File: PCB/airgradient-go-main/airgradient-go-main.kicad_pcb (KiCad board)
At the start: 4 copper layers, 62.9 x 87 mm, 165 parts, among them CN1 SM02B-SRSS-TB (LF)(SN), CN2 BM05B-SRSS-TB(LF)(SN), CN3 BM05B-SRSS-TB(LF)(SN), CN4 HCZZ0039-4, Q1 SIA445EDJ-T1-GE3, Q2 ZVN4106FTA_C508255, Q3 SS8050-G, Q4 SI1308EDL, SW1 TS-1091C-A1B3-D2, SW2 TS-1091C-A1B3-D2, U1 W25N512GVEIG, U10 TMUX121NKGR_C22428404, U11 LIS2DH12TR, U12 HYG-8503A, U13 SHT4x, U14 ZDSD512MLGEAG, U15 DPS368XTSA1, U16 TAU1113, U17 S12, U18 TCA9536DTMR, U2 TPS63802DLAR, U3 BQ25628RYKR, U4 ESP32-C5-MINI-1, U5 TPL5010DDCR, U7 TPS7A0228DQNR, U8 BQ27427YZFR, U9 SGP41-D-R4

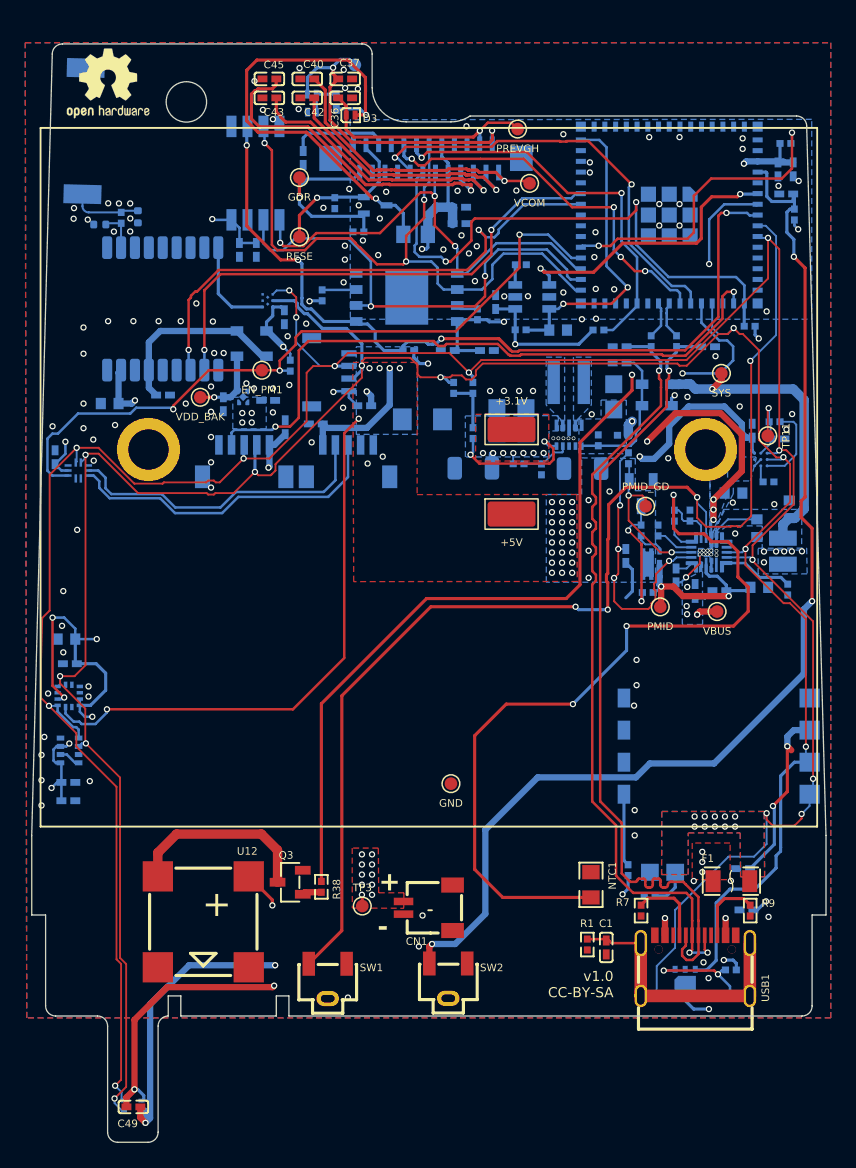
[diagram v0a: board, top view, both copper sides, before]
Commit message: Import v2.0 development state from Bitbucket branch v2.0
Overlay of the v2.0 design work onto the restructured PCB/ layout:
- airgradient-go-main v2.0 WIP: 186 footprints, microSD, PS1-CO,
  Birdy schematic review fixes; adds v2.0 BOM CSVs
- touch-pad v2.0: T1-T3 pads wired to touch controller CS channels,
  +3.1V rail renamed to VCC
- scd4x-module: minor updates
- libraries: new parts (SPL07-003, BM05B-SRSS-TB, PS1-CO, battery
  holder, ESP32-C5 models) and updated footprints; all library and
  3D model references normalized to ${KIPRJMOD}-relative paths
- led_pcb board was dropped in v2.0 (never migrated)

Known open items carried over from review: U14 VDD_IO not yet
connected to the 3.1V rail; U19 (LM66200) still fitted.
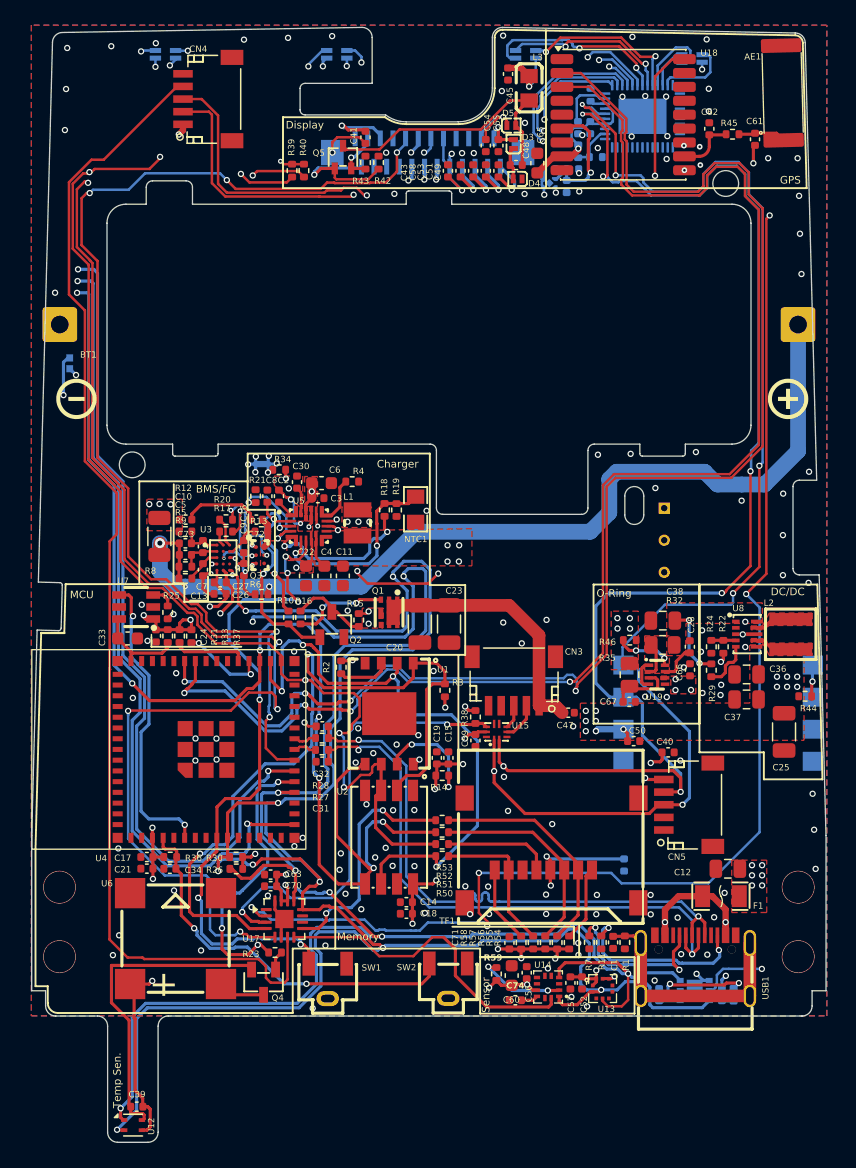
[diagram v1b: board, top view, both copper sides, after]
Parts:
- removed ANT1: GPS1003, easyeda2kicad:ANT-SMD_L10.0-W3.0
- removed CN1: SM02B-SRSS-TB (LF)(SN), easyeda2kicad:CONN-SMD_2P-P1.00_SM02B-SRSS-TB-LF-SN
- removed CN2: BM05B-SRSS-TB(LF)(SN), easyeda2kicad:CONN-SMD-5P-P1.00_BM05B-SRSS-TB-LF-SN
- removed D1, D2: PMEG3005EL,315, easyeda2kicad:SOD-882_L1.0-W0.6-RD
- removed D6, D7: CUS10S30,H3F, easyeda2kicad:SOD-323_L1.8-W1.3-LS2.5-RD
- removed the REF** at (106.6, 63.2)
- removed the REF** at (102.7, 126.9)
- removed the REF** at (134.0, 88.4)
- removed the REF** at (161.2, 126.9)
- removed TAB_BOTTOM, TAB_LEFT, TAB_RIGHT, TAB_TOP: Tab, Tab
- removed TP1: SYS, TestPoint:TestPoint_Pad_D1.0mm
- removed TP10: VDD_BAK, TestPoint:TestPoint_Pad_D1.0mm
- removed TP11: V1.8, TestPoint:TestPoint_Pad_D1.0mm
- removed TP13: GDR, TestPoint:TestPoint_Pad_D1.0mm
- removed TP14: RESE, TestPoint:TestPoint_Pad_D1.0mm
- removed TP15: PREVGH, TestPoint:TestPoint_Pad_D1.0mm
- removed TP16: PREVGL, TestPoint:TestPoint_Pad_D1.0mm
- removed TP17: VCOM, TestPoint:TestPoint_Pad_D1.0mm
- removed TP18: GND, TestPoint:TestPoint_Pad_D1.0mm
- removed TP3: PACK+, TestPoint:TestPoint_Pad_D1.0mm
- removed TP4: PMID_GD, TestPoint:TestPoint_Pad_D1.0mm
- removed TP5: +3.1V, TestPoint:TestPoint_Keystone_5019_Miniature
- removed TP6: PMID, TestPoint:TestPoint_Pad_D1.0mm
- removed TP7: VBUS, TestPoint:TestPoint_Pad_D1.0mm
- removed TP8: +5V, TestPoint:TestPoint_Keystone_5019_Miniature
- removed TP9: EN_PM1, TestPoint:TestPoint_Pad_D1.0mm
- added ?: , , F.Cu at (161.2, 132.4)
- added ?: , , F.Cu at (102.7, 132.4)
- added AE1: Antenna, AG-lib-oaf:CA-G01, F.Cu at (162.9, 63.9)
- added BT1: Battery_Cell, AG-lib-oaf:AGGO-battery, F.Cu at (131.0, 89.7)
- added C44: 1uF/50V, Capacitor_SMD:C_0402_1005Metric, B.Cu at (150.2, 135.4)
- added C61: DNP, Capacitor_SMD:C_0402_1005Metric, F.Cu at (157.8, 67.7)
- added C62: DNP, Capacitor_SMD:C_0402_1005Metric, F.Cu at (154.2, 66.8)
- added C63: 0.1uF/25V, Capacitor_SMD:C_0402_1005Metric, F.Cu at (119.4, 125.9)
- added C64: 1uF/50V, Capacitor_SMD:C_0402_1005Metric, B.Cu at (142.9, 71.4)
- added C65: 10uF/25V, Capacitor_SMD:C_0603_1608Metric, F.Cu at (140.6, 69.5)
- added C66: 1uF/50V, Capacitor_SMD:C_0402_1005Metric, F.Cu at (152.6, 109.7)
- added C67: 1uF/50V, Capacitor_SMD:C_0402_1005Metric, F.Cu at (147.8, 112.2)
- added C68: 1uF/50V, Capacitor_SMD:C_0402_1005Metric, B.Cu at (143.8, 66.7)
- added C69: 0.1uF/16V, Capacitor_SMD:C_0402_1005Metric, B.Cu at (144.7, 66.7)
- added C70: 0.1uF/25V, Capacitor_SMD:C_0402_1005Metric, F.Cu at (119.4, 126.8)
- added C71: 0.1uF/25V, Capacitor_SMD:C_0402_1005Metric, F.Cu at (138.3, 131.3)
- added C72: 0.1uF/25V, Capacitor_SMD:C_0402_1005Metric, F.Cu at (118.3, 97.8)
- added C73: 0.1uF/25V, Capacitor_SMD:C_0402_1005Metric, F.Cu at (112.7, 97.8)
- added C74: 0.1uF/25V, Capacitor_SMD:C_0402_1005Metric, F.Cu at (138.8, 135.8)
- added CN5: SM05B-SRSS-TB (LF)(SN), easyeda2kicad-oaf:CONN-SMD_SM05B-SRSS-TB-LF-SN, F.Cu at (152.5, 120.3)
- added G***: LOGO, LOGO, F.Cu at (160.4, 88.2)
- added G***: LOGO, LOGO, F.Cu at (104.1, 88.2)
- added G***: LOGO, LOGO, B.Cu at (160.4, 88.2)
- added G***: LOGO, LOGO, B.Cu at (104.1, 88.2)
- added LED1: TJ-S1608SW6TDSLCCYRGB-A5, easyeda2kicad-oaf:LED-ARRAY-SMD_4P-L1.6-W0.8-BL-FD, B.Cu at (111.1, 60.9)
- added LED2: TJ-S1608SW6TDSLCCYRGB-A5, easyeda2kicad-oaf:LED-ARRAY-SMD_4P-L1.6-W0.8-BL-FD, B.Cu at (124.7, 60.9)
- added LED3: TJ-S1608SW6TDSLCCYRGB-A5, easyeda2kicad-oaf:LED-ARRAY-SMD_4P-L1.6-W0.8-BL-FD, B.Cu at (139.6, 60.9)
- added LED4: TJ-S1608SW6TDSLCCYRGB-A5, easyeda2kicad-oaf:LED-ARRAY-SMD_4P-L1.6-W0.8-BL-FD, B.Cu at (152.8, 61.2)
- added NT1: NetTie_2, NetTie:NetTie-2_SMD_Pad0.5mm, B.Cu at (118.7, 93.4)
- added NTC2: NCP15XH103F03RC, easyeda2kicad-oaf:R0402, B.Cu at (103.5, 85.4)
- added Q5: SI1308EDL, easyeda2kicad-oaf:SOT-323-3_L2.0-W1.3-P1.30-LS2.1-BR, F.Cu at (125.2, 69.1)
- added R15: 15K, Resistor_SMD:R_0402_1005Metric, F.Cu at (126.4, 105.7)
- added R40: 100K, Resistor_SMD:R_0402_1005Metric, F.Cu at (122.1, 70.1)
- added R41: 4.7R, Resistor_SMD:R_0402_1005Metric, B.Cu at (156.1, 135.4)
- added R42: 1M, Resistor_SMD:R_0402_1005Metric, F.Cu at (128.0, 69.5)
- added R43: 2.2R, Resistor_SMD:R_0402_1005Metric, F.Cu at (126.9, 69.5)
- added R44: 100K, Resistor_SMD:R_0402_1005Metric, F.Cu at (161.8, 111.8)
- added R45: 0R, Resistor_SMD:R_0402_1005Metric, F.Cu at (156.0, 67.2)
- added R46: 100K, Resistor_SMD:R_0402_1005Metric, F.Cu at (147.9, 107.3)
- added R47: 0R, Resistor_SMD:R_0402_1005Metric, B.Cu at (143.8, 68.6)
- added R48: 0R, Resistor_SMD:R_0402_1005Metric, B.Cu at (145.2, 69.1)
- added R49: 5.1K, Resistor_SMD:R_0402_1005Metric, B.Cu at (144.8, 64.1)
- added R50: 22R, Resistor_SMD:R_0402_1005Metric, F.Cu at (133.0, 124.4)
- added R51: 22R, Resistor_SMD:R_0402_1005Metric, F.Cu at (133.0, 123.5)
- added R52: 22R, Resistor_SMD:R_0402_1005Metric, F.Cu at (133.0, 122.5)
- added R53: 22R, Resistor_SMD:R_0402_1005Metric, F.Cu at (133.0, 121.6)
- added R54: 10K, Resistor_SMD:R_0402_1005Metric, F.Cu at (143.1, 131.3)
- added R55: 10K, Resistor_SMD:R_0402_1005Metric, F.Cu at (142.1, 131.3)
- added R56: 10K, Resistor_SMD:R_0402_1005Metric, F.Cu at (141.2, 131.3)
- added R57: 10K, Resistor_SMD:R_0402_1005Metric, F.Cu at (140.2, 131.3)
- added R58: 10K, Resistor_SMD:R_0402_1005Metric, F.Cu at (139.3, 131.3)
- added R59: 100K, Resistor_SMD:R_0402_1005Metric, F.Cu at (137.3, 133.8)
- added TF1: TF-CARD XG8P H1.5, easyeda2kicad-oaf:TF-SMD_TF-CARD-XG8P-H1.5, F.Cu at (141.7, 124.0)
- added U19: LM66200DRLR, easyeda2kicad-oaf:SOT-583-8_L2.1-W1.2-P0.50-LS1.6-BL, F.Cu at (150.0, 110.1)
- added U20: LP5036, Package_DFN_QFN:VQFN-46-1EP_5x6mm_P0.4mm_EP2.8x3.8mm, B.Cu at (148.9, 65.8)
- added U6: HYG-8503A, easyeda2kicad-oaf:BUZ-SMD_4P-L8.5-W8.5-P8.50-BR, F.Cu at (111.9, 130.9)
- C1, C35, C40, C43: footprint easyeda2kicad:C0402 -> Capacitor_SMD:C_0402_1005Metric
- C10, C7: value 10uF/10V -> 0.1uF/25V; footprint easyeda2kicad:C0402 -> Capacitor_SMD:C_0402_1005Metric; moved to F.Cu
- C11, C4: footprint easyeda2kicad:C0603 -> Capacitor_SMD:C_0603_1608Metric; moved to F.Cu
- C12: value 0.1uF/25V -> 22uF/25V; footprint easyeda2kicad:C0402 -> Capacitor_SMD:C_0805_2012Metric; moved to F.Cu
- C13, C5: value 22uF/25V -> 0.1uF/25V; footprint easyeda2kicad:C0805 -> Capacitor_SMD:C_0402_1005Metric; moved to F.Cu
- C14, C19, C2, C26, C41, C55: footprint easyeda2kicad:C0402 -> Capacitor_SMD:C_0402_1005Metric; moved to F.Cu
- C15, C3, C59: value 10uF/25V -> 0.1uF/25V; footprint easyeda2kicad:C0603 -> Capacitor_SMD:C_0402_1005Metric; moved to F.Cu
- C16: value 4.7uF/25V -> 0.1uF/25V; footprint easyeda2kicad:C0402 -> Capacitor_SMD:C_0402_1005Metric; moved to F.Cu
- C17: value 22uF/25V -> 0.1uF/10V; footprint easyeda2kicad:C0805 -> Capacitor_SMD:C_0402_1005Metric; moved to F.Cu
- C18: value DNP -> 1uF/50V; footprint Capacitor_SMD:C_1206_3216Metric -> Capacitor_SMD:C_0402_1005Metric; moved to F.Cu
- C20: footprint easyeda2kicad:C1206 -> Capacitor_SMD:C_1206_3216Metric; moved to F.Cu
- C21: value 1nF/50V -> 22uF/10V; footprint easyeda2kicad:C0402 -> Capacitor_SMD:C_0402_1005Metric; moved to F.Cu
- C22: value 1nF/50V -> 10uF/25V; footprint easyeda2kicad:C0402 -> Capacitor_SMD:C_0603_1608Metric; moved to F.Cu
- C23: value 500pF/50V -> DNP; footprint easyeda2kicad:C0603 -> Capacitor_SMD:C_1206_3216Metric; moved to F.Cu
- C24: value DNP -> 0.1uF/25V; footprint Capacitor_SMD:C_1206_3216Metric -> Capacitor_SMD:C_0402_1005Metric; moved to F.Cu
- C25: value 10nF/10V -> DNP; footprint easyeda2kicad:C0402 -> Capacitor_SMD:C_1206_3216Metric; moved to F.Cu
- C27: value 1uF/50V -> 0.47uF/25V; footprint easyeda2kicad:C0402 -> Capacitor_SMD:C_0402_1005Metric; moved to F.Cu
- C28: value 2.2uF/16V -> 0.1uF/25V; footprint easyeda2kicad:C0402 -> Capacitor_SMD:C_0402_1005Metric; moved to F.Cu
- C29, C46, C49: value 0.1uF/25V -> 1uF/50V; footprint easyeda2kicad:C0402 -> Capacitor_SMD:C_0402_1005Metric
- C30: value 4.7uF/25V -> 1uF/50V; footprint easyeda2kicad:C0402 -> Capacitor_SMD:C_0402_1005Metric; moved to F.Cu
- C31: value 1uF/50V -> 1nF/50V; footprint easyeda2kicad:C0402 -> Capacitor_SMD:C_0402_1005Metric; moved to F.Cu
- C32: value 4.7uF/25V -> 1nF/50V; footprint easyeda2kicad:C0402 -> Capacitor_SMD:C_0402_1005Metric; moved to F.Cu
- C33: value 0.1uF/25V -> 500pF/50V; footprint easyeda2kicad:C0402 -> Capacitor_SMD:C_0603_1608Metric; moved to F.Cu
- C34: value 1uF/50V -> 10nF/10V; footprint easyeda2kicad:C0402 -> Capacitor_SMD:C_0402_1005Metric; moved to F.Cu
- C36, C37: value 1uF/50V -> 22uF/25V; footprint easyeda2kicad:C0402 -> Capacitor_SMD:C_0805_2012Metric
- C38: value 1uF/50V -> 22uF/25V; footprint easyeda2kicad:C0402 -> Capacitor_SMD:C_0805_2012Metric; moved to F.Cu
- C39, C52, C56, C57, C9: value 1uF/50V -> 0.1uF/25V; footprint easyeda2kicad:C0402 -> Capacitor_SMD:C_0402_1005Metric; moved to F.Cu
- C42: footprint easyeda2kicad:C0402 -> Capacitor_SMD:C_0402_1005Metric; moved to B.Cu
- C45: value 1uF/50V -> 4.7uF/25V; footprint easyeda2kicad:C0402 -> Capacitor_SMD:C_0402_1005Metric
- C47, C51: value DNP -> 1uF/50V; moved to F.Cu
- C48: value 1uF/50V -> 4.7uF/25V; footprint easyeda2kicad:C0402 -> Capacitor_SMD:C_0402_1005Metric; moved to F.Cu
- C50, C54, C58: value 0.1uF/25V -> 1uF/50V; footprint easyeda2kicad:C0402 -> Capacitor_SMD:C_0402_1005Metric; moved to F.Cu
- C53: value 10uF/25V -> 1uF/50V; footprint easyeda2kicad:C0603 -> Capacitor_SMD:C_0402_1005Metric; moved to F.Cu
- C6, C60: value 0.1uF/25V -> 10uF/25V; footprint easyeda2kicad:C0402 -> Capacitor_SMD:C_0603_1608Metric; moved to F.Cu
- C8: value 22uF/25V -> 4.7uF/25V; footprint easyeda2kicad:C0805 -> Capacitor_SMD:C_0402_1005Metric; moved to F.Cu
- CN3: value BM05B-SRSS-TB(LF)(SN) -> SM05B-SRSS-TB (LF)(SN); footprint easyeda2kicad:CONN-SMD-5P-P1.00_BM05B-SRSS-TB-LF-SN -> easyeda2kicad-oaf:CONN-SMD_SM05B-SRSS-TB-LF-SN; moved to F.Cu
- CN4: value HCZZ0039-4 -> SM05B-SRSS-TB (LF)(SN); footprint easyeda2kicad:CONN-SMD_HCZZ0039-4 -> easyeda2kicad-oaf:CONN-SMD_SM05B-SRSS-TB-LF-SN; moved to F.Cu
- D3: footprint easyeda2kicad:SOD-882_L1.0-W0.6-RD -> easyeda2kicad-oaf:SOD-882_L1.0-W0.6-RD
- D4, D5: value CUS10S30,H3F -> PMEG3005EL,315; footprint easyeda2kicad:SOD-323_L1.8-W1.3-LS2.5-RD -> easyeda2kicad-oaf:SOD-882_L1.0-W0.6-RD; moved to F.Cu
- F1: footprint easyeda2kicad:F1206 -> easyeda2kicad-oaf:F1206
- FPC1: footprint easyeda2kicad:FPC-SMD_FPC-0.5-24P-LTH2.0 -> easyeda2kicad-oaf:FPC-SMD_FPC-0.5-24P-LTH2.0
- L1: footprint easyeda2kicad:IND-SMD_L2.5-W2.0 -> easyeda2kicad-oaf:IND-SMD_L2.5-W2.0; moved to F.Cu
- L2: footprint easyeda2kicad:IND-SMD_L4.0-W4.0_XGL4020 -> easyeda2kicad-oaf:IND-SMD_L4.0-W4.0_XGL4020; moved to F.Cu
- L3: footprint easyeda2kicad:L0805 -> easyeda2kicad-oaf:L0805; moved to F.Cu
- NTC1: footprint easyeda2kicad:R0805 -> easyeda2kicad-oaf:R0805
- Q1: footprint easyeda2kicad:SC-70-6L_L2.0-W2.0-P0.65-BL -> easyeda2kicad-oaf:SC-70-6L_L2.0-W2.0-P0.65-BL; moved to F.Cu
- Q2: footprint easyeda2kicad:SOT-23-3_L2.9-W1.3-P1.90-LS2.4-BR -> easyeda2kicad-oaf:SOT-23-3_L2.9-W1.3-P1.90-LS2.4-BR; moved to F.Cu
- Q3: value SS8050-G -> CSD83325L; footprint easyeda2kicad:SOT-23-3_L2.9-W1.3-P1.90-LS2.4-BR -> easyeda2kicad-oaf:PICOSTAR-6_L2.2-W1.1-R2-C3-P0.65-BL
- Q4: value SI1308EDL -> SS8050-G; footprint easyeda2kicad:SOT-323-3_L2.0-W1.3-P1.30-LS2.1-BR -> easyeda2kicad-oaf:SOT-23-3_L2.9-W1.3-P1.90-LS2.4-BR; moved to F.Cu
- R1, R7: footprint easyeda2kicad:R0402 -> Resistor_SMD:R_0402_1005Metric
- R10, R14, R2, R26, R3, R30, R31, R33, R36, R37: footprint easyeda2kicad:R0402 -> Resistor_SMD:R_0402_1005Metric; moved to F.Cu
- R11: value 4.12K -> 5.1K; footprint easyeda2kicad:R0402 -> Resistor_SMD:R_0402_1005Metric; moved to F.Cu
- R12: value 17.33K -> 200R; footprint easyeda2kicad:R0402 -> Resistor_SMD:R_0402_1005Metric; moved to F.Cu
- R13: value 2.49K -> 2K; footprint easyeda2kicad:R0402 -> Resistor_SMD:R_0402_1005Metric; moved to F.Cu
- R16: value 51K -> 20K; footprint easyeda2kicad:R0402 -> Resistor_SMD:R_0402_1005Metric; moved to F.Cu
- R17: value 15K -> 1K; footprint easyeda2kicad:R0402 -> Resistor_SMD:R_0402_1005Metric; moved to F.Cu
- R18: value 20K -> 4.12K; footprint easyeda2kicad:R0402 -> Resistor_SMD:R_0402_1005Metric; moved to F.Cu
- R19: value 10K -> 17.33K; footprint easyeda2kicad:R0402 -> Resistor_SMD:R_0402_1005Metric; moved to F.Cu
- R20: value 22R -> 1K; footprint easyeda2kicad:R0402 -> Resistor_SMD:R_0402_1005Metric; moved to F.Cu
- R21: value 22R -> 2.49K; footprint easyeda2kicad:R0402 -> Resistor_SMD:R_0402_1005Metric; moved to F.Cu
- R22: value 10K -> 475K; footprint easyeda2kicad:R0402 -> Resistor_SMD:R_0402_1005Metric; moved to F.Cu
- R23: value 100K -> 1K; footprint easyeda2kicad:R0402 -> Resistor_SMD:R_0402_1005Metric; moved to F.Cu
- R24: value 10K -> 91K; footprint easyeda2kicad:R0402 -> Resistor_SMD:R_0402_1005Metric; moved to F.Cu
- R25: value 0R -> 51K; footprint easyeda2kicad:R0402 -> Resistor_SMD:R_0402_1005Metric; moved to F.Cu
- R27, R28: value 10K -> 22R; footprint easyeda2kicad:R0402 -> Resistor_SMD:R_0402_1005Metric; moved to F.Cu
- R29, R39: value 0R -> 100K; footprint easyeda2kicad:R0402 -> Resistor_SMD:R_0402_1005Metric; moved to F.Cu
- R32: value 1M -> 50mR; footprint easyeda2kicad:R0402 -> Resistor_SMD:R_0805_2012Metric; moved to F.Cu
- R34: value 2.2R -> 10K; footprint easyeda2kicad:R0402 -> Resistor_SMD:R_0402_1005Metric; moved to F.Cu
- R35: value 4.7R -> 470mR; footprint easyeda2kicad:R0402 -> Resistor_SMD:R_0805_2012Metric; moved to F.Cu
- R38: value 1K -> 100K; footprint easyeda2kicad:R0402 -> Resistor_SMD:R_0402_1005Metric
- R4: value 475K -> 100K; footprint easyeda2kicad:R0402 -> Resistor_SMD:R_0402_1005Metric; moved to F.Cu
- R5: value 100K -> 200R; footprint easyeda2kicad:R0402 -> Resistor_SMD:R_0402_1005Metric; moved to F.Cu
- R6: value 91K -> 10R; footprint easyeda2kicad:R0402 -> Resistor_SMD:R_0402_1005Metric; moved to F.Cu
- R8: value 100K -> 5mR 1%/1W; footprint easyeda2kicad:R0402 -> Resistor_SMD:R_1206_3216Metric; moved to F.Cu
- R9: value 5.1K -> 10R; footprint easyeda2kicad:R0402 -> Resistor_SMD:R_0402_1005Metric
- REF**: footprint AG-lib:GO-enclosure -> AG-lib-oaf:GO-enclosure
- REF**: footprint SPS30:SPS30 -> SPS30-oaf:SPS30
- SW1, SW2: footprint easyeda2kicad:KEY-SMD_3P-L5.5-W3.8-P3.00 -> easyeda2kicad-oaf:KEY-SMD_3P-L5.5-W3.8-P3.00
- U1: footprint easyeda2kicad:WSON-8_L8.0-W6.0-P1.27-TL-1 -> easyeda2kicad-oaf:WSON-8_L8.0-W6.0-P1.27-TL-1; moved to F.Cu
- U10: value TMUX121NKGR_C22428404 -> SGP41-D-R4; footprint easyeda2kicad:UQFN-10_L1.8-W1.4-P0.40-BL -> Senserion-oaf:XDCR_SGP41-D-R4
- U11: value LIS2DH12TR -> PS1-CO-SMOKE-10k; footprint easyeda2kicad:LGA-12_L2.0-W2.0-P0.50-BL -> AG-lib-oaf:PS1-CO-SMOKE-10k
- U12: value HYG-8503A -> SHT4x; footprint easyeda2kicad:BUZ-SMD_4P-L8.5-W8.5-P8.50-BR -> Sensor_Humidity:Sensirion_DFN-4_1.5x1.5mm_P0.8mm_SHT4x_NoCentralPad
- U13: value SHT4x -> SPL07-003; footprint Sensor_Humidity:Sensirion_DFN-4_1.5x1.5mm_P0.8mm_SHT4x_NoCentralPad -> easyeda2kicad-oaf:LGA-10_L2.0-W2.0-P0.50-BL; moved to F.Cu
- U14: value ZDSD512MLGEAG -> LIS2DH12TR; footprint easyeda2kicad:LGA-8_L8.0-W6.0-P1.27-TL -> easyeda2kicad-oaf:LGA-12_L2.0-W2.0-P0.50-BL; moved to F.Cu
- U15: value DPS368XTSA1 -> TMUX121NKGR_C22428404; footprint easyeda2kicad:LGA-8_L2.5-W2.0-P0.65-TR_DPS368 -> easyeda2kicad-oaf:UQFN-10_L1.8-W1.4-P0.40-BL; moved to F.Cu
- U16: value TAU1113 -> S12; footprint RF_GPS:TAU1113 -> S12-oaf:S12
- U17: value S12 -> TCA6408ARGT; footprint S12:S12 -> Package_DFN_QFN:VQFN-16-1EP_3x3mm_P0.5mm_EP1.45x1.45mm; moved to F.Cu
- U18: value TCA9536DTMR -> TAU1113; footprint easyeda2kicad:X2SON-8_L1.4-W0.8-P0.50-BL -> RF_GPS-oaf:TAU1113; moved to F.Cu
- U2: value TPS63802DLAR -> ZDSD512MLGEAG; footprint easyeda2kicad:VSON-10_L3.0-W2.0-P0.50-TL -> easyeda2kicad-oaf:LGA-8_L8.0-W6.0-P1.27-TL; moved to F.Cu
- U3: value BQ25628RYKR -> BQ27742YZFR-G1; footprint easyeda2kicad:WQFN-18_L3.0-W2.5-P0.40-TL -> easyeda2kicad-oaf:DSBGA-15_L2.6-W2.0-R5-C3-P0.50-BL; moved to F.Cu
- U4: footprint Esparessif:ESP32-C5-MINI-1 -> Esparessif-oaf:ESP32-C5-MINI-1; moved to F.Cu
- U5: value TPL5010DDCR -> BQ25628RYKR; footprint easyeda2kicad:SOT-23-6_L2.9-W1.6-P0.95-LS2.8-BR -> easyeda2kicad-oaf:WQFN-18_L3.0-W2.5-P0.40-TL; moved to F.Cu
- U7: value TPS7A0228DQNR -> TPL5010DDCR; footprint easyeda2kicad:X2SON-4_L1.0-W1.0-P0.65-TL-EP -> easyeda2kicad-oaf:SOT-23-6_L2.9-W1.6-P0.95-LS2.8-BR; moved to F.Cu
- U8: value BQ27427YZFR -> TPS63802DLAR; footprint easyeda2kicad:DSBGA-9_L1.6-W1.6-R3-C3-P0.50-TL -> easyeda2kicad-oaf:VSON-10_L3.0-W2.0-P0.50-TL; moved to F.Cu
- U9: value SGP41-D-R4 -> TPS7A0228DQNR; footprint Senserion:XDCR_SGP41-D-R4 -> easyeda2kicad-oaf:X2SON-4_L1.0-W1.0-P0.65-TL-EP
- USB1: footprint easyeda2kicad:USB-C-SMD_G-SWITCH_GT-USB-7010ASV -> easyeda2kicad-oaf:USB-C-SMD_G-SWITCH_GT-USB-7010ASV
- moved C49 79.6 mm to (137.5, 70.2), turned to -90 degrees
- moved U14 68.5 mm to (141.4, 134.8), turned to 90 degrees
- moved C41 68.2 mm to (126.9, 67.5), turned to 90 degrees
- moved R26 68.1 mm to (116.7, 125.4), turned to 0 degrees
- moved C46 67.8 mm to (155.2, 135.4)
- moved U4 66.7 mm to (106.6, 115.8), turned to 90 degrees
- moved C42 65.7 mm to (147.4, 125.1), turned to 90 degrees
- moved U9 64.3 mm to (141.5, 71.1), turned to 180 degrees
- moved U10 63.9 mm to (153.0, 135.1)
- moved Q4 62.2 mm to (118.9, 134.4), turned to 90 degrees
- moved U11 60.9 mm to (163.1, 99.4), turned to -90 degrees
- moved C21 60.7 mm to (109.6, 125.4), turned to 0 degrees
- moved C40 60.5 mm to (150.9, 116.2), turned to 180 degrees
- moved C58 58.8 mm to (134.5, 70.2), turned to -90 degrees
- moved C37 58.5 mm to (157.1, 112.0), turned to 0 degrees
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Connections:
- C10 pad 1: GND -> Net-(U3-SRP)
- C10 pad 2: +3.1V -> /BAT+
- C11 pad 2: Load+ -> SYS
- C12 pad 2: PMID -> VBUS
- C13 pad 1: GND -> Net-(U3-VPWR)
- C13 pad 2: +3.1V -> /BAT-
- C15 pad 2: PMID -> +3.1V
- C16 pad 1: GND -> Net-(U3-PACKP)
- C16 pad 2: /REGN -> /BAT-
- C17 pad 2: Net-(U2-VIN) -> +3.1V
- C18 pad 1: +3.1V -> GND
- C18 pad 2: GND -> +3.1V
- C19 pad 2: VBUS -> +3.1V
- C21 pad 2: /USB_D- -> +3.1V
- C22 pad 2: /USB_D+ -> Pack+
- C23 pad 1: GND -> +5V
- C23 pad 2: /EN -> GND
- C24 pad 1: +5V -> GND
- C24 pad 2: GND -> +3.1V
- C25 pad 1: GND -> +3.1V
- C25 pad 2: /IO28 -> GND
- C26 pad 1: GND -> /BAT-
- C26 pad 2: PACK+ -> Net-(U3-REG25)
- C27 pad 1: GND -> Net-(U3-REG25)
- C27 pad 2: VDD_BAK -> Net-(U3-TS)
- C28 pad 1: V1.8 -> GND
- C28 pad 2: GND -> Net-(C28-Pad2)
- C29 pad 2: Net-(D6-K) -> VDD_BAK
- C3 pad 2: SYS -> PMID
- C30 pad 2: +3.1V -> VBUS
- C31 pad 2: Load+ -> /USB_D-
- C32 pad 1: Net-(Q4-D) -> GND
- C32 pad 2: Net-(C32-Pad2) -> /USB_D+
- C33 pad 2: +3.1V -> /EN
- C34 pad 2: Net-(C34-Pad2) -> /IO28
- C35 pad 2: +3.1V -> Pack+
- C36 pad 2: /PREVGH -> +3.1V
- C37 pad 2: /PREVGL -> +3.1V
- C38 pad 2: +3.1V -> Net-(U8-EN)
- C39 pad 2: Net-(U9-VDD) -> +3.1V
- C40 pad 2: /VCOM -> +3.1V
- C41 pad 2: +3.1V -> Net-(C41-Pad2)
- C42 pad 2: Net-(C42-Pad2) -> +3.1V
- C43 pad 2: Net-(C43-Pad2) -> +3.1V
- C45 pad 2: Net-(C45-Pad2) -> +3.1V
- C47 pad 1: Net-(ANT1-Pad1) -> GND
- C47 pad 2: GND -> +5V
- C48 pad 1: GND -> Net-(Q5-D)
- C48 pad 2: +3.1V -> Net-(C48-Pad2)
- C49 pad 2: +3.1V -> /VCOM
- C5 pad 1: GND -> /BAT+
- C5 pad 2: VBUS -> Net-(U3-SRN)
- C51 pad 1: /GNSS_RF -> GND
- C51 pad 2: GND -> Net-(C51-Pad2)
- C53 pad 2: +3.1V -> Net-(C53-Pad2)
- C54 pad 2: +3.1V -> /PREVGH
- C55 pad 2: Net-(D4-K) -> /PREVGL
- C56 pad 2: +5V -> +3.1V
- C58 pad 2: +3.1V -> Net-(C58-Pad2)
- C6 pad 2: +3.1V -> PMID
- C7 pad 1: GND -> Net-(U3-SRP)
- C7 pad 2: +3.1V -> Net-(U3-SRN)
- C8 pad 2: +3.1V -> /REGN
- C9 pad 1: GND -> Net-(U3-BAT)
- C9 pad 2: +3.1V -> /BAT-
- CN3 pad 1: GND -> +5V
- CN3 pad 2: GND -> /PM_SDA
- CN3 pad 4: /PM_SDA -> GND
- CN3 pad 5: +5V -> GND
- CN4 pad 4: GND -> /INT
- D3 pad 1: /PREVGH -> Net-(C48-Pad2)
- D3 pad 2: Net-(Q4-D) -> /PREVGL
- D4 pad 1: Net-(D4-K) -> GND
- D4 pad 2: VDD_BAK -> Net-(C48-Pad2)
- D5 pad 1: Net-(D4-K) -> /PREVGH
- D5 pad 2: +3.1V -> Net-(Q5-D)
- FPC1 pad 18: Net-(C45-Pad2) -> Net-(C58-Pad2)
- FPC1 pad 20: Net-(C43-Pad2) -> Net-(C53-Pad2)
- FPC1 pad 22: Net-(C42-Pad2) -> Net-(C51-Pad2)
- FPC1 pad 5: Net-(C34-Pad2) -> Net-(C41-Pad2)
- L2 pad 1: Net-(U2-L1) -> Net-(U8-L1)
- L2 pad 2: Net-(U2-L2) -> Net-(U8-L2)
- L3 pad 2: Net-(Q4-D) -> Net-(Q5-D)
- NTC1 pad 2: Net-(U3-TS) -> Net-(U5-TS)
- Q4 pad 1: /GDR -> Net-(Q4-B)
- Q4 pad 2: /RESE -> GND
- Q4 pad 3: Net-(Q4-D) -> Net-(Q4-C)
- R10 pad 1: Net-(U1-/HOLD(IO3)) -> /REGN
- R10 pad 2: +3.1V -> /PMID_GD
- R11 pad 1: Net-(U3-TS) -> GND
- R11 pad 2: Net-(U3-TS_BIAS) -> Net-(USB1-CC2)
- R12 pad 1: GND -> Net-(C73-Pad2)
- R12 pad 2: Net-(U3-TS) -> Net-(U3-SRP)
- R13 pad 1: GND -> Pack+
- R13 pad 2: Net-(U3-ILIM) -> Net-(U3-PACKP)
- R14 pad 1: /REGN -> Net-(U1-/HOLD(IO3))
- R14 pad 2: /PMID_GD -> +3.1V
- R16 pad 1: GND -> Net-(Q2-D)
- R16 pad 2: Net-(U5-DELAY/M_RST) -> Net-(Q1-G)
- R17 pad 1: PMID -> Net-(U3-CHG)
- R17 pad 2: Net-(Q2-D) -> Net-(Q3-G-PadB1)
- R18 pad 1: Net-(Q2-D) -> Net-(U5-TS)
- R18 pad 2: Net-(Q1-G) -> Net-(U5-TS_BIAS)
- R19 pad 1: /SDA -> GND
- R19 pad 2: +3.1V -> Net-(U5-TS)
- R20 pad 1: /USB_D- -> Net-(U3-DSG)
- R20 pad 2: /USB- -> Net-(Q3-G-PadB2)
- R21 pad 1: /USB_D+ -> GND
- R21 pad 2: /USB+ -> Net-(U5-ILIM)
- R22 pad 1: /SCL -> Net-(U8-FB)
- R23 pad 1: /EN -> /BUZZ
- R23 pad 2: +3.1V -> Net-(Q4-B)
- R24 pad 1: /IO27 -> Net-(U8-FB)
- R24 pad 2: +3.1V -> GND
- R25 pad 1: Net-(D6-K) -> GND
- R25 pad 2: Net-(U2-VIN) -> Net-(U7-DELAY/M_RST)
- R26 pad 1: /IO28 -> /SDA
- R27 pad 1: /EN_PM1 -> /USB_D-
- R27 pad 2: +3.1V -> /USB-
- R28 pad 1: Net-(U8-BIN) -> /USB+
- R28 pad 2: GND -> /USB_D+
- R29 pad 1: Net-(U2-VIN) -> Net-(U8-EN)
- R29 pad 2: Load+ -> Net-(U8-PG)
- R30 pad 1: V1.8 -> /SCL
- R30 pad 2: Net-(U8-GPOUT) -> +3.1V
- R31 pad 1: +3.1V -> /EN
- R31 pad 2: /ePaper CS -> +3.1V
- R32 pad 1: GND -> Net-(C28-Pad2)
- R32 pad 2: /GDR -> Net-(U8-EN)
- R33 pad 1: +3.1V -> /IO27
- R33 pad 2: /ePaper D/C -> +3.1V
- R34 pad 2: /RESE -> VBUS
- R35 pad 1: Net-(U9-VDD) -> VBUS
- R35 pad 2: +3.1V -> Net-(U19-VIN1)
- R36 pad 1: GND -> /IO28
- R36 pad 2: VBUS -> +3.1V
- R37 pad 1: Net-(U17-EN) -> /IO26
- R38 pad 1: /BUZZ -> /EN_PM1
- R38 pad 2: Net-(Q3-B) -> +3.1V
- R39 pad 1: Net-(ANT1-Pad1) -> +3.1V
- R39 pad 2: /GNSS_RF -> /ePaper CS
- R4 pad 1: Net-(U2-FB) -> GND
- R4 pad 2: +3.1V -> /CE
- R5 pad 1: GND -> /BAT+
- R5 pad 2: /CE -> Net-(U3-SRN)
- R6 pad 1: Net-(U2-FB) -> /BAT+
- R6 pad 2: GND -> Net-(U3-BAT)
- R8 pad 1: +3.1V -> /BAT+
- R8 pad 2: Net-(U2-PG) -> Net-(C73-Pad2)
- R9 pad 1: GND -> /BAT+
- R9 pad 2: Net-(USB1-CC2) -> Net-(U3-VPWR)
- U10 pad 1: /SCL -> Net-(U10-VDD)
- U10 pad 2: /SDA -> GND
- U10 pad 3: GND -> /SDA
- U10 pad 4: /PM_SDA -> GND
- U10 pad 5: /PM_SCL -> +3.1V
- U10 pad 6: unconnected-(U10-S2B-Pad6) -> /SCL
- U10 pad 7: unconnected-(U10-S1B-Pad7) -> GND
- U11 pad 1: /SCL -> unconnected-(U11-R-Pad1)
- U11 pad 2: +3.1V -> unconnected-(U11-S-Pad2)
- U11 pad 3: GND -> unconnected-(U11-C-Pad3)
- U12 pad 1: +3.1V -> /SDA
- U12 pad 2: Net-(Q3-C) -> /SCL
- U12 pad 3: unconnected-(U12-NC-Pad3) -> +3.1V
- U12 pad 4: unconnected-(U12-NC-Pad4) -> GND
- U13 pad 1: /SDA -> +3.1V
- U13 pad 3: +3.1V -> GND
- U13 pad 4: GND -> /SDA
- U14 pad 1: unconnected-(U14-DATA2-Pad1) -> /SCL
- U14 pad 2: /NAND CS -> Net-(U14-CS)
- U14 pad 3: /SCLK -> GND
- U14 pad 4: GND -> /SDA
- U14 pad 5: /MOSI -> GND
- U14 pad 6: /MISO -> GND
- U14 pad 7: unconnected-(U14-DATA1-Pad7) -> GND
- U14 pad 8: +3.1V -> GND
- U15 pad 1: GND -> /SCL
- U15 pad 2: unconnected-(U15-CSB-Pad2) -> /SDA
- U15 pad 3: /SDA -> GND
- U15 pad 4: /SCL -> /PM_SDA
- U15 pad 5: unconnected-(U15-SDO-Pad5) -> /PM_SCL
- U15 pad 6: +3.1V -> unconnected-(U15-S2B-Pad6)
- U15 pad 7: GND -> unconnected-(U15-S1B-Pad7)
- U15 pad 8: +3.1V -> /EN_PM1
- U16 pad 2: /MCU_RX -> +3.1V
- U16 pad 3: /MCU_TX -> /SDA
- U16 pad 4: unconnected-(U16-PPS-Pad4) -> /SCL
- U16 pad 5: unconnected-(U16-EXTINT-Pad5) -> Net-(U16-EN)
- U16 pad 6: Net-(D4-K) -> unconnected-(U16-DE-Pad6)
- U16 pad 8: +3.1V -> GND
- U17 pad 1: GND -> unconnected-(U17-~{RESET}-Pad1)
- U17 pad 2: +3.1V -> /PRTRG
- U17 pad 3: /SDA -> /EN_PM1
- U17 pad 4: /SCL -> /NAND CS
- U17 pad 5: Net-(U17-EN) -> /ePaper D/C
- U17 pad 6: unconnected-(U17-DE-Pad6) -> GND
- U17 pad 7: unconnected-(U17-RDYN-Pad7) -> /INT
- U17 pad 8: GND -> /ACC_INT
- U18 pad 1: /PRTRG -> GND
- U18 pad 2: unconnected-(U18-P2-Pad2) -> /MCU_RX
- U18 pad 3: GND -> /MCU_TX
- U18 pad 5: /SCL -> unconnected-(U18-EXTINT-Pad5)
- U18 pad 6: /SDA -> VDD_BAK
- U18 pad 7: +3.1V -> unconnected-(U18-RESERVED-Pad7)
- U18 pad 8: unconnected-(U18-P1-Pad8) -> +3.1V
- U2 pad 1: Net-(D6-K) -> unconnected-(U2-DATA2-Pad1)
- U2 pad 2: GND -> /NAND CS
- U2 pad 3: GND -> /SCLK
- U2 pad 4: Net-(U2-FB) -> GND
- U2 pad 5: Net-(U2-PG) -> /MOSI
- U2 pad 6: +3.1V -> /MISO
- U2 pad 7: Net-(U2-L2) -> unconnected-(U2-DATA1-Pad7)
- U2 pad 8: GND -> +3.1V
- U4 pad 17: /INT -> /IO1
- U4 pad 26: /ePaper D/C -> /IO15
- U4 pad 34: /EN_PM1 -> /IO26
- U4 pad 7: /ACC_INT -> /IO3
- U4 pad 8: /NAND CS -> /IO4
- U5 pad 1: +3.1V -> /BTST
- U5 pad 2: GND -> /REGN
- U5 pad 3: Net-(U5-DELAY/M_RST) -> /PMID_GD
- U5 pad 4: /WD_RST -> Net-(U5-ILIM)
- U5 pad 5: unconnected-(U5-WAKE-Pad5) -> Net-(U5-TS_BIAS)
- U5 pad 6: /EN -> Net-(U5-TS)
- U7 pad 1: VDD_BAK -> +3.1V
- U7 pad 3: Load+ -> Net-(U7-DELAY/M_RST)
- U7 pad 4: Load+ -> /WD_RST
- U7 pad 5: GND -> unconnected-(U7-WAKE-Pad5)
- U9 pad 1: Net-(U9-VDD) -> VDD_BAK
- U9 pad 3: /SDA -> Pack+
- U9 pad 4: GND -> Pack+
- U9 pad 5: +3.1V -> GND
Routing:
- net /SDA: track 206.1 -> 341.5 mm, vias 11 -> 17
- net /SCL: track 222.7 -> 350.0 mm, vias 14 -> 18
- net /PRTRG: track 7.60 -> 124.8 mm, vias 0 -> 6
- net /MOSI: track 36.4 -> 142.9 mm, vias 3 -> 8
- net /ePaper D/C: track 31.5 -> 128.2 mm, vias 2 -> 7
- net Pack+: track 0.00 -> 92.7 mm, vias 0 -> 4
- net /BAT+: track 0.00 -> 76.9 mm, vias 0 -> 3
- net /MCU_RX: track 40.5 -> 115.9 mm, vias 2 -> 4
- net /MCU_TX: track 42.3 -> 113.8 mm, vias 2 -> 4
- net /ePaper RES: track 34.7 -> 104.9 mm, vias 2 -> 3
- net /ePaper CS: track 44.1 -> 109.4 mm, vias 2 -> 4
- net /ACC_INT: track 90.2 -> 25.7 mm, vias 3 -> 0
- net /SCLK: track 50.5 -> 110.4 mm, vias 3 -> 6
- net /IO28: track 89.1 -> 30.8 mm, vias 3 -> 2
- net /ePaper BUSY: track 30.5 -> 86.9 mm, vias 4 -> 5
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- added copper zone on In2.Cu, net +3.1V
- added copper zone on In1.Cu, net /BAT-
- added copper zone on F.Cu, net /SW
- added copper zone on In2.Cu, net /SW
- added copper zone on In1.Cu, net GND
- added copper zone on F.Cu, net Net-(C28-Pad2)
- added copper zone on F.Cu, net Net-(C73-Pad2)
- added copper zone on In2.Cu, net Net-(C73-Pad2)
- added copper zone on F.Cu, net Net-(U8-EN)
- added copper zone on F.Cu, net Net-(U8-L1)
- added copper zone on F.Cu, net Net-(U8-L2)
- added copper zone on F.Cu, net PMID
- added copper zone on In2.Cu, net PMID
- added copper zone on F.Cu, net Pack+
- added copper zone on F.Cu, net SYS
- added copper zone on In2.Cu, net SYS
- added copper zone on In2.Cu, net VBUS
- removed copper zone on In1.Cu, net (none)
- removed copper zone on In2.Cu, net (none)
- removed copper zone on B.Cu, net +3.1V
- removed copper zone on In1.Cu, net +3.1V
- removed copper zone on B.Cu, net +5V
- removed copper zone on F.Cu, net +5V
- removed copper zone on B.Cu, net /SW
- removed copper zone on In1.Cu, net /SW
- removed copper zone on B.Cu, net Load+
- removed copper zone on F.Cu, net Net-(F1-Pad1)
- removed copper zone on In1.Cu, net Net-(F1-Pad1)
- removed copper zone on B.Cu, net Net-(U2-L1)
- removed copper zone on B.Cu, net Net-(U2-L2)
- removed copper zone on B.Cu, net Net-(U2-VIN)
- removed copper zone on F.Cu, net PACK+
- removed copper zone on In1.Cu, net PACK+
- removed copper zone on B.Cu, net SYS
- removed copper zone on B.Cu, net VBUS
- removed copper zone on In1.Cu, net VBUS
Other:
- board size 62.9 x 87 mm -> 62.9 x 88.3 mm
- board text added: "BMS/FG"
- board text added: "Charger"
- board text added: "DC/DC"
- board text added: "Display"
- board text added: "GPS"
- board text added: "GPS_BAK"
- board text added: "LED Control"
- board text added: "MCU"
- board text added: "Memory"
- board text added: "O-Ring"
- board text added: "Sensor"
- board text added: "TVOC"
- board text added: "Temp Sen."
- board text removed: "+"
- board text removed: "-"
- board text removed: "Power"
- board text removed: "v1.0 CC-BY-SA"
- board text removed: "{ "ViaStitching": "0.2", "stitch_zone_0": { "HSpacing": "0.1", "VSpacing": "0.1", "HOffset": "0", "VOffset": "0", "Clearance": "0", "Randomize": false } }"
- board text removed: "{ "ViaStitching": "0.2", "stitch_zone_0": { "HSpacing": "0.3", "VSpacing": "0.3", "HOffset": "0", "VOffset": "0", "Clearance": "0", "Randomize": false } }"
- board text removed: "{ "ViaStitching": "0.2", "stitch_zone_0": { "HSpacing": "0.7", "VSpacing": "0.7", "HOffset": "0", "VOffset": "0", "Clearance": "0", "Randomize": false } }"
- board text removed: "{ "ViaStitching": "0.2", "stitch_zone_0": { "HSpacing": "1", "VSpacing": "1", "HOffset": "0", "VOffset": "0", "Clearance": "0", "Randomize": false } }"
- board text removed: "{ "ViaStitching": "0.2", "stitch_zone_0": { "HSpacing": "5", "VSpacing": "5", "HOffset": "0", "VOffset": "0", "Clearance": "0", "Randomize": false } }"

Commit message: Rework main PCB layout: ESP32-C5 placement, routing, and silkscreen
- Move ESP32-C5 module further inward from the board edge and rework affected track routing
- Improve reference designator silkscreen placement
- Restore SD card section (DNP)
- Add OSHW and AirGradient logos and version label
- Move Q5 closer to L3
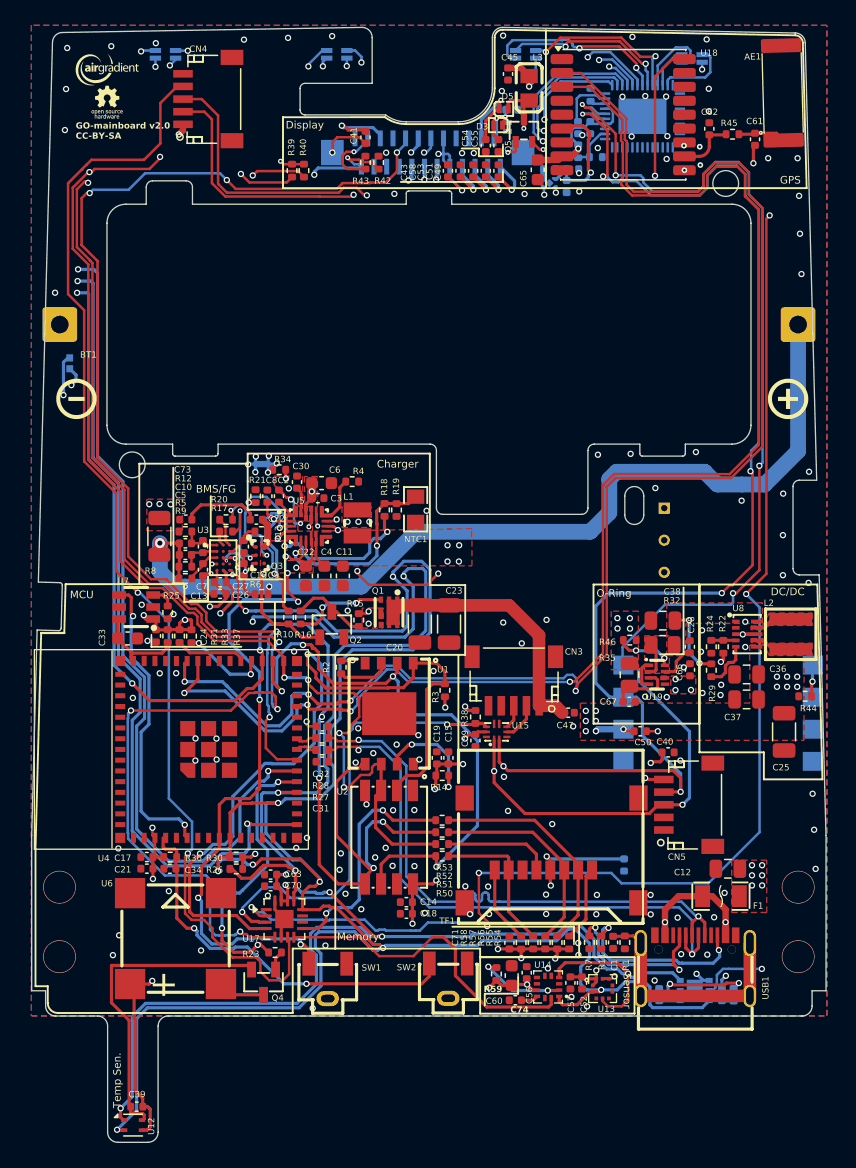
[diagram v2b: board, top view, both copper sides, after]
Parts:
- added G***: LOGO, LOGO, F.Cu at (106.5, 64.7)
- added G***: LOGO, LOGO, F.Cu at (106.5, 62.1)
- C48, D4: moved to B.Cu
- moved Q5 14.5 mm to (139.5, 67.0)
- moved C48 4.39 mm to (138.5, 65.3)
- moved D4 4.20 mm to (138.2, 66.7), turned to 90 degrees
- moved D3 1.93 mm to (137.5, 66.5), turned to 180 degrees
- moved D5 1.45 mm to (137.9, 65.2)
- moved C50 0.94 mm to (148.7, 114.5)
- moved C65 0.53 mm to (140.6, 70.1), turned to 90 degrees
- moved U4 0.20 mm to (106.8, 115.8)
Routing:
- net /RESE: track 4.20 -> 22.2 mm, vias 1 -> 2
- net Net-(Q5-D): track 22.3 -> 6.45 mm, vias 0 -> 1
- net /GDR: track 10.6 -> 23.1 mm, vias 1 -> 3
- net /INT: track 93.5 -> 90.9 mm, vias 0 -> 2
- net Net-(U3-REG25): track 32.4 -> 30.4 mm
- net /PREVGH: track 6.04 -> 7.37 mm
- net Net-(U3-TS): track 31.8 -> 30.6 mm
- net GND: track 45.6 -> 46.5 mm, vias 144 -> 145
- net Net-(C48-Pad2): track 2.62 -> 1.79 mm, vias 0 -> 1
- net /NAND CS: track 60.1 -> 60.7 mm
- net Net-(C73-Pad2): track 0.83 -> 1.40 mm
- net /BUZZ: track 22.4 -> 21.9 mm
- net /SCLK: track 110.4 -> 110.1 mm, vias 6 -> 7
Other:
- board text added: "GO-mainboard v2.0 CC-BY-SA"
